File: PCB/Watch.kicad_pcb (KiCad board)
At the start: 2 copper layers, 37 x 39.8 mm, 48 parts, among them J1 USB_C_Receptacle_USB2.0_14P, Q1 2N3904, Q2 2N3904, Q3 2N3904, Q4 2N3904, SW1 SW_Push, SW3 SW_Push, SW4 SW_Push, U1 MCP73831-2-OT, U3 AP2112K-3.3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

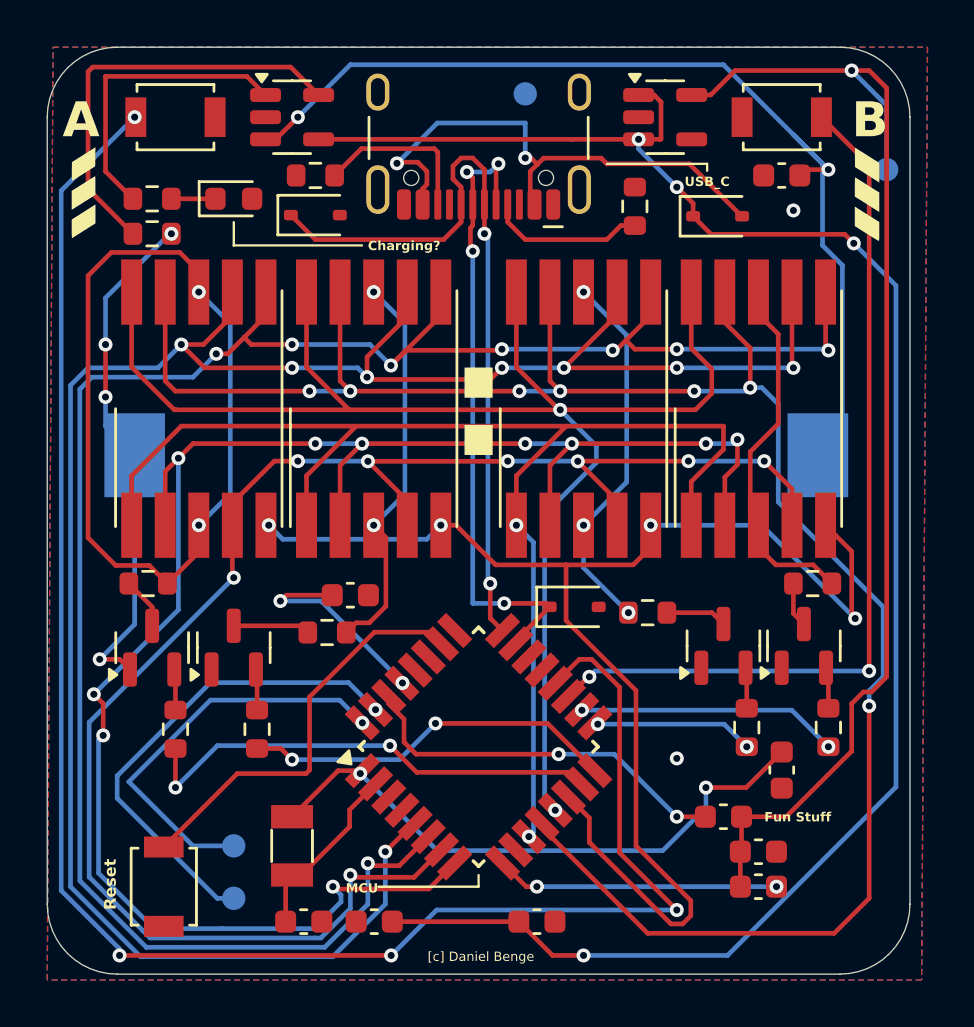
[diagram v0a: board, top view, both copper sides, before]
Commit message: Switch regulator
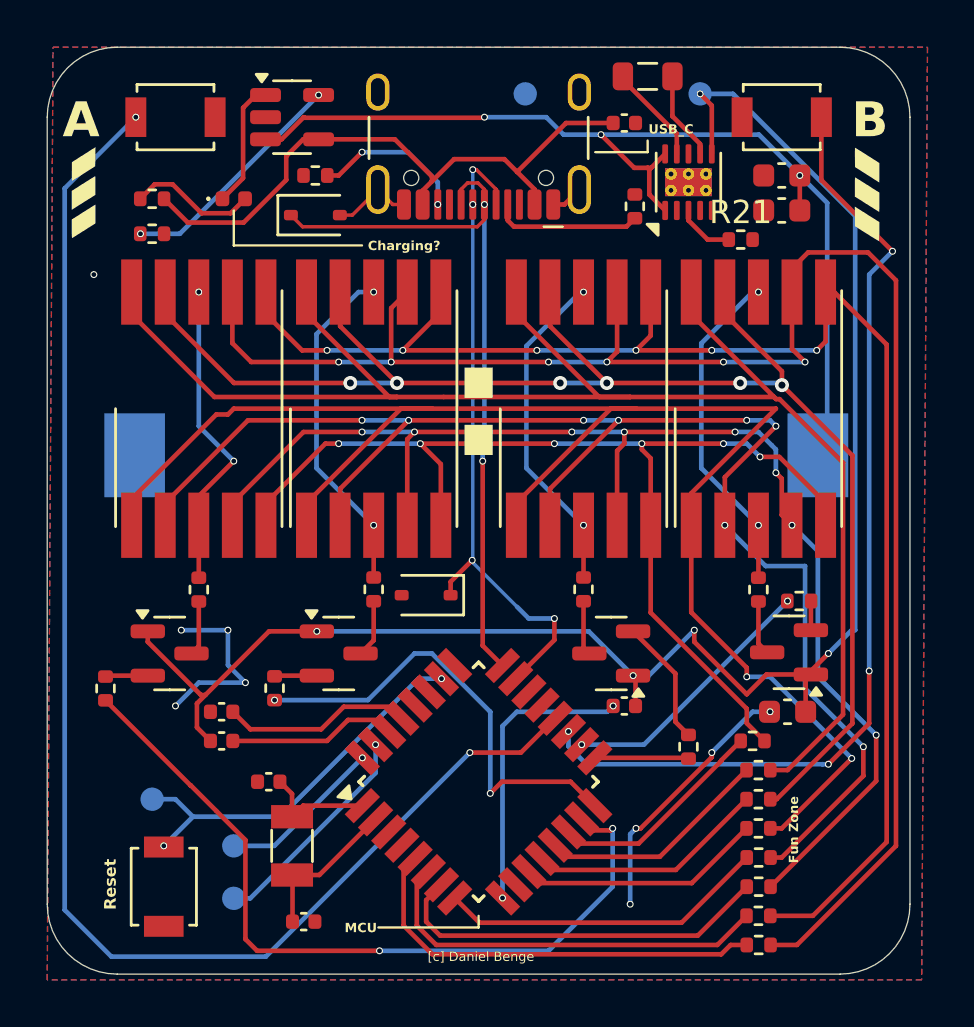
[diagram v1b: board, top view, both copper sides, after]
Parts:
- removed C2, C4: 4.7µF, Capacitor_SMD:C_0603_1608Metric
- removed D76: D_Schottky_Small, Diode_SMD:D_SOD-323
- removed U3: AP2112K-3.3, Package_TO_SOT_SMD:SOT-23-5
- added C_IN1: 10uF, Capacitor_SMD:C_0603_1608Metric, F.Cu at (190.5, 87.0)
- added C_OUT1: 22uF, Capacitor_SMD:C_0603_1608Metric, F.Cu at (190.8, 108.5)
- added L1: 2.2uH, Inductor_SMD:L_0805_2012Metric, F.Cu at (184.8, 81.2)
- added R13: 150, Resistor_SMD:R_0402_1005Metric, F.Cu at (189.5, 114.8)
- added R14: 150, Resistor_SMD:R_0402_1005Metric, F.Cu at (189.5, 116.0)
- added R15: 150, Resistor_SMD:R_0402_1005Metric, F.Cu at (189.5, 117.2)
- added R16: 150, Resistor_SMD:R_0402_1005Metric, F.Cu at (189.5, 118.5)
- added R17: 390, Resistor_SMD:R_0402_1005Metric, F.Cu at (161.5, 107.5)
- added R18: 390, Resistor_SMD:R_0402_1005Metric, F.Cu at (168.8, 107.5)
- added R19: 390, Resistor_SMD:R_0402_1005Metric, F.Cu at (186.5, 110.0)
- added R20: 390, Resistor_SMD:R_0402_1005Metric, F.Cu at (191.2, 103.8)
- added R21: 36.5k, Resistor_SMD:R_0402_1005Metric, F.Cu at (188.7, 88.2)
- added TP5: TestPoint, TestPoint:TestPoint_Pad_D1.0mm, B.Cu at (163.5, 112.2)
- added U2: TPS63900, Package_SON:WSON-10-1EP_2.5x2.5mm_P0.5mm_EP1.2x2mm_ThermalVias, F.Cu at (186.5, 85.8)
- C1, C10, C5, C6, C7, C9: footprint Capacitor_SMD:C_0603_1608Metric -> Capacitor_SMD:C_0402_1005Metric
- D3: footprint LED_SMD:LED_0603_1608Metric -> LED_SMD:LED_0402_1005Metric
- Q1, Q2, Q3, Q4: value 2N3904 -> 2N3906
- R1, R10, R11, R12, R2, R3, R4, R5: footprint Resistor_SMD:R_0603_1608Metric -> Resistor_SMD:R_0402_1005Metric
- R6, R7, R8, R9: value 1k -> 150; footprint Resistor_SMD:R_0603_1608Metric -> Resistor_SMD:R_0402_1005Metric
- moved C7 35.9 mm to (183.8, 83.2), turned to 180 degrees
- moved R8 25.2 mm to (189.5, 112.2), turned to 180 degrees
- moved C9 22.0 mm to (168.5, 111.5), turned to 180 degrees
- moved C5 21.8 mm to (166.5, 109.8), turned to 180 degrees
- moved R6 21.3 mm to (189.2, 109.8), turned to 180 degrees
- moved C6 9.65 mm to (183.8, 108.2), turned to 0 degrees
- moved TP1 8.63 mm to (187.0, 82.0)
- moved C1 7.45 mm to (166.5, 108.5), turned to 180 degrees
- moved D2 6.37 mm to (175.2, 103.5), turned to 180 degrees
- moved R9 5.26 mm to (189.5, 113.5), turned to 180 degrees
- moved Q3 4.82 mm to (183.2, 106.0), turned to 180 degrees
- moved Q2 4.51 mm to (171.5, 106.0), turned to 0 degrees
- moved R11 2.93 mm to (182.0, 103.2), turned to 90 degrees
- moved R10 2.72 mm to (173.0, 103.2), turned to 90 degrees
- moved R12 2.34 mm to (189.5, 103.3), turned to 90 degrees
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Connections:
- net Net-(BT1-+) renamed VBAT
- net Net-(U7-~{RESET}) renamed TP_RST
- D3 pad 2: GND -> Net-(D3-A)
- J1 pad A4: Net-(D76-A) -> +5V
- J1 pad A9: Net-(D76-A) -> +5V
- J1 pad B4: Net-(D76-A) -> +5V
- J1 pad B9: Net-(D76-A) -> +5V
- Q1 pad 1: GND -> TP_3.3V
- Q2 pad 1: GND -> TP_3.3V
- Q3 pad 1: GND -> TP_3.3V
- Q4 pad 1: GND -> TP_3.3V
- R4 pad 1: Net-(U1-STAT) -> Net-(D3-A)
- R4 pad 2: Net-(D3-K) -> +5V
- R6 pad 1: SEL-D2 -> DP
- R6 pad 2: Net-(Q2-B) -> Net-(U7-PA11)
- R7 pad 1: SEL-D3 -> G
- R7 pad 2: Net-(Q3-B) -> Net-(U7-PA10)
- R8 pad 1: SEL-D1 -> F
- R8 pad 2: Net-(Q1-B) -> Net-(U7-PA09)
- R9 pad 1: SEL-D4 -> E
- R9 pad 2: Net-(Q4-B) -> Net-(U7-PA08)
- U1 pad 1: Net-(U1-STAT) -> Net-(D3-K)
- U7 pad 11: E -> Net-(U7-PA08)
- U7 pad 12: F -> Net-(U7-PA09)
- U7 pad 13: G -> Net-(U7-PA10)
- U7 pad 14: DP -> Net-(U7-PA11)
- U7 pad 5: A -> Net-(U7-PA04)
- U7 pad 6: B -> Net-(U7-PA05)
- U7 pad 7: C -> Net-(U7-PA06)
- U7 pad 8: D -> Net-(U7-PA07)
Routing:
- net +5V: track 78.3 -> 27.0 mm, vias 4 -> 0
- net Net-(D76-A): track 23.2 -> 0.00 mm, vias 2 -> 0
- net Net-(Dig1-CA-Pad3): track 36.0 -> 13.5 mm
- net B: track 86.1 -> 65.0 mm, vias 8 -> 6
- net A0: track 25.5 -> 4.93 mm, vias 2 -> 0
- net F: track 84.1 -> 64.1 mm, vias 7 -> 6
- net TP_3.3V: track 52.2 -> 71.9 mm, vias 1 -> 5
- net Net-(U7-PA04): track 0.00 -> 18.5 mm
- net Net-(U7-PA05): track 0.00 -> 17.5 mm
- net Net-(U7-PA06): track 0.00 -> 16.7 mm
- net Btn2: track 77.3 -> 61.4 mm, vias 4 -> 2
- net A: track 89.3 -> 74.4 mm, vias 8 -> 6
- net C: track 71.0 -> 56.5 mm
- net Net-(U7-PA07): track 0.00 -> 14.1 mm
- net E: track 57.2 -> 70.8 mm
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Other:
- board text added: "Fun Zone"
- board text added: "RST"
- board text removed: "Fun Stuff"

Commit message: Fix charge LED, display resistors
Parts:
- removed R10, R11, R12, R5: 150, Resistor_SMD:R_0402_1005Metric
- turned D3 to 180 degrees
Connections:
- Dig1 pad 3: Net-(Dig1-CA-Pad3) -> DIG1
- Dig1 pad 8: Net-(Dig1-CA-Pad3) -> DIG1
- Dig2 pad 3: Net-(Dig2-CA-Pad3) -> DIG2
- Dig2 pad 8: Net-(Dig2-CA-Pad3) -> DIG2
- Dig3 pad 3: Net-(Dig3-CA-Pad3) -> DIG3
- Dig3 pad 8: Net-(Dig3-CA-Pad3) -> DIG3
- Dig4 pad 3: Net-(Dig4-CA-Pad3) -> DIG4
- Dig4 pad 8: Net-(Dig4-CA-Pad3) -> DIG4
- R4 pad 1: Net-(D3-A) -> Net-(D3-K)
- U1 pad 1: Net-(D3-K) -> Net-(D3-A)
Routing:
- net DIG2: track 2.47 -> 18.1 mm, vias 0 -> 2
- net DIG4: track 2.34 -> 17.8 mm, vias 0 -> 2
- net DIG3: track 2.34 -> 17.7 mm, vias 0 -> 2
- net Net-(Dig2-CA-Pad3): track 14.7 -> 0.00 mm, vias 2 -> 0
- net DIG1: track 2.36 -> 16.9 mm, vias 0 -> 2
- net Net-(Dig4-CA-Pad3): track 14.4 -> 0.00 mm, vias 2 -> 0
- net Net-(Dig3-CA-Pad3): track 14.3 -> 0.00 mm, vias 2 -> 0
- net Net-(Dig1-CA-Pad3): track 13.5 -> 0.00 mm, vias 2 -> 0

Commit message: Add resistor to reset button, small schematic changes
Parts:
- added R5: 10k, Resistor_SMD:R_0402_1005Metric, F.Cu at (163.0, 112.2)
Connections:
- SW1 pad 2: TP_RST -> Net-(R5-Pad1)
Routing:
- net Net-(R5-Pad1): track 0.00 -> 2.73 mm
- net TP_RST: track 17.0 -> 15.2 mm
